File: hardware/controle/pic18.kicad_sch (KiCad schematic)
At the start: 10 parts, among them J10 Conn_01x05_Pin, J11 PWM, J12 ADC, U5 PIC18F05Q40

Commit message: controle: - pass ERC - adjust some components and connections - place components on board
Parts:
- J10: footprint conn-local:Molex_Pico-SPOX-5-Vertical -> Connector_PinHeader_2.54mm:PinHeader_1x05_P2.54mm_Horizontal
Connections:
- net +3.3V: now also J10.2 (Pin_2); no longer J10.5 (Pin_5)
- net GND: now also J10.3 (Pin_3); no longer J10.2 (Pin_2)
- net PGC: now also J10.5 (Pin_5); no longer J10.3 (Pin_3)
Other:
- moved on the sheet: J10, R20
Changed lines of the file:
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@@
 	)
 	(junction
-		(at 116.84 83.82)
+		(at 106.68 83.82)
 		(diameter 0)
 		(color 0 0 0 0)
 	)
 	(junction
-		(at 114.3 92.71)
+		(at 106.68 95.25)
+		(diameter 0)
+		(color 0 0 0 0)
+	)
+	(junction
+		(at 111.76 95.25)
 		(diameter 0)
 		(color 0 0 0 0)
@@
 	)
 	(junction
-		(at 109.22 88.9)
-		(diameter 0)
-		(color 0 0 0 0)
-	)
-	(junction
 		(at 157.48 88.9)
 		(diameter 0)
@@
 	(wire
 		(pts
-			(xy 116.84 83.82) (xy 157.48 83.82)
-		)
-		(stroke
-			(width 0)
-			(type default)
-		)
-	)
-	(wire
-		(pts
 			(xy 118.11 137.16) (xy 110.49 137.16)
 		)
@@
 	(wire
 		(pts
-			(xy 114.3 104.14) (xy 114.3 92.71)
-		)
-		(stroke
-			(width 0)
-			(type default)
-		)
-	)
-	(wire
-		(pts
 			(xy 93.98 111.76) (xy 140.97 111.76)
 		)
@@
 	(wire
 		(pts
-			(xy 140.97 106.68) (xy 111.76 106.68)
+			(xy 140.97 106.68) (xy 114.3 106.68)
 		)
 		(stroke
@@
 	(wire
 		(pts
-			(xy 109.22 92.71) (xy 109.22 88.9)
-		)
-		(stroke
-			(width 0)
-			(type default)
-		)
-	)
-	(wire
-		(pts
 			(xy 93.98 88.9) (xy 99.06 88.9)
 		)
@@
 	(wire
 		(pts
+			(xy 104.14 80.01) (xy 93.98 80.01)
+		)
+		(stroke
+			(width 0)
+			(type default)
+		)
+	)
+	(wire
+		(pts
 			(xy 104.14 88.9) (xy 106.68 88.9)
 		)
@@
 	(wire
 		(pts
-			(xy 106.68 80.01) (xy 93.98 80.01)
-		)
-		(stroke
-			(width 0)
-			(type default)
-		)
-	)
-	(wire
-		(pts
 			(xy 118.11 132.08) (xy 118.11 137.16)
 		)
@@
 	(wire
 		(pts
-			(xy 106.68 88.9) (xy 106.68 92.71)
-		)
-		(stroke
-			(width 0)
-			(type default)
-		)
-	)
-	(wire
-		(pts
-			(xy 116.84 80.01) (xy 116.84 83.82)
+			(xy 106.68 83.82) (xy 157.48 83.82)
+		)
+		(stroke
+			(width 0)
+			(type default)
+		)
+	)
+	(wire
+		(pts
+			(xy 106.68 88.9) (xy 106.68 95.25)
+		)
+		(stroke
+			(width 0)
+			(type default)
+		)
+	)
+	(wire
+		(pts
+			(xy 114.3 80.01) (xy 114.3 106.68)
+		)
+		(stroke
+			(width 0)
+			(type default)
+		)
+	)
+	(wire
+		(pts
+			(xy 111.76 104.14) (xy 140.97 104.14)
+		)
+		(stroke
+			(width 0)
+			(type default)
+		)
+	)
+	(wire
+		(pts
+			(xy 106.68 80.01) (xy 106.68 83.82)
+		)
+		(stroke
+			(width 0)
+			(type default)
+		)
+	)
+	(wire
+		(pts
+			(xy 109.22 80.01) (xy 109.22 88.9)
 		)
 		(stroke
@@
 	(wire
 		(pts
-			(xy 140.97 104.14) (xy 114.3 104.14)
+			(xy 106.68 95.25) (xy 106.68 99.06)
 		)
 		(stroke
@@
 	(wire
 		(pts
-			(xy 111.76 80.01) (xy 111.76 106.68)
-		)
-		(stroke
-			(width 0)
-			(type default)
-		)
-	)
-	(wire
-		(pts
-			(xy 114.3 92.71) (xy 114.3 80.01)
+			(xy 111.76 104.14) (xy 111.76 95.25)
 		)
 		(stroke
@@
 	(wire
 		(pts
-			(xy 104.14 83.82) (xy 116.84 83.82)
+			(xy 111.76 80.01) (xy 111.76 95.25)
+		)
+		(stroke
+			(width 0)
+			(type default)
+		)
+	)
+	(wire
+		(pts
+			(xy 104.14 83.82) (xy 106.68 83.82)
 		)
 		(stroke
@@
 		(pts
 			(xy 93.98 83.82) (xy 99.06 83.82)
-		)
-		(stroke
-			(width 0)
-			(type default)
-		)
-	)
-	(wire
-		(pts
-			(xy 109.22 88.9) (xy 109.22 80.01)
 		)
 		(stroke
@@
 	)
 	(symbol
-		(lib_id "centrale-rescue:GND-power")
+		(lib_id "power:GND")
 		(at 116.84 139.7 90)
 		(unit 1)
@@
 					(size 1.27 1.27)
 				)
+				(hide yes)
 			)
 		)
@@
 					(size 1.27 1.27)
 				)
-			)
-		)
-		(property "Description" ""
+				(hide yes)
+			)
+		)
+		(property "Description" "Power symbol creates a global label with name \"GND\" , ground"
 			(at 116.84 139.7 0)
 			(effects
@@
 	(symbol
 		(lib_id "power:GND")
-		(at 106.68 92.71 0)
+		(at 106.68 99.06 0)
 		(unit 1)
 		(exclude_from_sim no)
@@
 		(fields_autoplaced yes)
 		(property "Reference" "#PWR023"
+			(at 106.68 105.41 0)
+			(effects
+				(font
+					(size 1.27 1.27)
+				)
+				(hide yes)
+			)
+		)
+		(property "Value" "GND"
+			(at 106.68 102.2349 90)
+			(effects
+				(font
+					(size 1.27 1.27)
+				)
+				(justify right)
+			)
+		)
+		(property "Footprint" ""
 			(at 106.68 99.06 0)
 			(effects
@@
 			)
 		)
-		(property "Value" "GND"
-			(at 106.68 95.8849 90)
-			(effects
-				(font
-					(size 1.27 1.27)
-				)
-				(justify right)
-			)
-		)
-		(property "Footprint" ""
-			(at 106.68 92.71 0)
-			(effects
-				(font
-					(size 1.27 1.27)
-				)
-				(hide yes)
-			)
-		)
 		(property "Datasheet" ""
-			(at 106.68 92.71 0)
+			(at 106.68 99.06 0)
 			(effects
 				(font
@@
 		)
 		(property "Description" "Power symbol creates a global label with name \"GND\" , ground"
-			(at 106.68 92.71 0)
+			(at 106.68 99.06 0)
 			(effects
 				(font
@@
 		)
 		(property "P/N" ""
-			(at 106.68 92.71 0)
+			(at 106.68 99.06 0)
 			(effects
 				(font
@@
 	(symbol
 		(lib_id "Connector:Conn_01x05_Pin")
-		(at 111.76 74.93 90)
+		(at 109.22 74.93 90)
 		(mirror x)
 		(unit 1)
@@
 		(dnp no)
 		(property "Reference" "J10"
-			(at 112.9722 74.2188 0)
+			(at 110.4322 74.2188 0)
 			(effects
 				(font
@@
 		)
 		(property "Value" "Conn_01x05_Pin"
-			(at 110.5479 74.2188 0)
+			(at 108.0079 74.2188 0)
 			(effects
 				(font
@@
 			)
 		)
-		(property "Footprint" "conn-local:Molex_Pico-SPOX-5-Vertical"
-			(at 111.76 74.93 0)
+		(property "Footprint" "Connector_PinHeader_2.54mm:PinHeader_1x05_P2.54mm_Horizontal"
+			(at 109.22 74.93 0)
 			(effects
 				(font
@@
 		)
 		(property "Datasheet" "~"
-			(at 111.76 74.93 0)
+			(at 109.22 74.93 0)
 			(effects
 				(font
@@
 		)
 		(property "Description" "Generic connector, single row, 01x05, script generated"
-			(at 111.76 74.93 0)
+			(at 109.22 74.93 0)
 			(effects
 				(font
@@
 		)
 		(property "P/N" "87437-0543"
-			(at 111.76 74.93 0)
+			(at 109.22 74.93 0)
 			(effects
 				(font
@@
 	)
 	(symbol
-		(lib_id "centrale-rescue:+3.3V-power")
+		(lib_id "power:+3.3V")
 		(at 130.81 142.24 270)
 		(unit 1)
@@
 			)
 		)
-		(property "Description" ""
+		(property "Description" "Power symbol creates a global label with name \"+3.3V\""
 			(at 130.81 142.24 0)
 			(effects
@@
 	(symbol
 		(lib_id "Device:R_Small")
-		(at 111.76 92.71 270)
+		(at 109.22 95.25 270)
 		(unit 1)
 		(exclude_from_sim no)
@@
 		(dnp no)
 		(property "Reference" "R20"
-			(at 111.76 94.742 90)
+			(at 109.22 97.282 90)
 			(effects
 				(font
@@
 		)
 		(property "Value" "10K"
-			(at 111.7854 92.8878 90)
+			(at 109.2454 95.4278 90)
 			(effects
 				(font
@@
 		)
 		(property "Footprint" "Resistor_SMD:R_0805_2012Metric_Pad1.20x1.40mm_HandSolder"
-			(at 111.76 90.932 90)
+			(at 109.22 93.472 90)
 			(effects
 				(font
@@
 		)
 		(property "Datasheet" "~"
-			(at 111.76 92.71 0)
+			(at 109.22 95.25 0)
 			(effects
 				(font
@@
 		)
 		(property "Description" "Resistor, small symbol"
-			(at 111.76 92.71 0)
+			(at 109.22 95.25 0)
 			(effects
 				(font
@@
 		)
 		(property "P/N" "stock"
-			(at 111.76 92.71 0)
+			(at 109.22 95.25 0)
 			(effects
 				(font
@@
 	)
 	(symbol
-		(lib_id "centrale-rescue:+3.3V-power")
+		(lib_id "power:+3.3V")
 		(at 113.03 142.24 270)
 		(unit 1)
@@
 			)
 		)
-		(property "Description" ""
+		(property "Description" "Power symbol creates a global label with name \"+3.3V\""
 			(at 113.03 142.24 0)
 			(effects
@@
 	)
 	(symbol
-		(lib_id "centrale-rescue:GND-power")
+		(lib_id "power:GND")
 		(at 134.62 139.7 90)
 		(unit 1)
@@
 					(size 1.27 1.27)
 				)
+				(hide yes)
 			)
 		)
@@
 					(size 1.27 1.27)
 				)
-			)
-		)
-		(property "Description" ""
+				(hide yes)
+			)
+		)
+		(property "Description" "Power symbol creates a global label with name \"GND\" , ground"
 			(at 134.62 139.7 0)
 			(effects

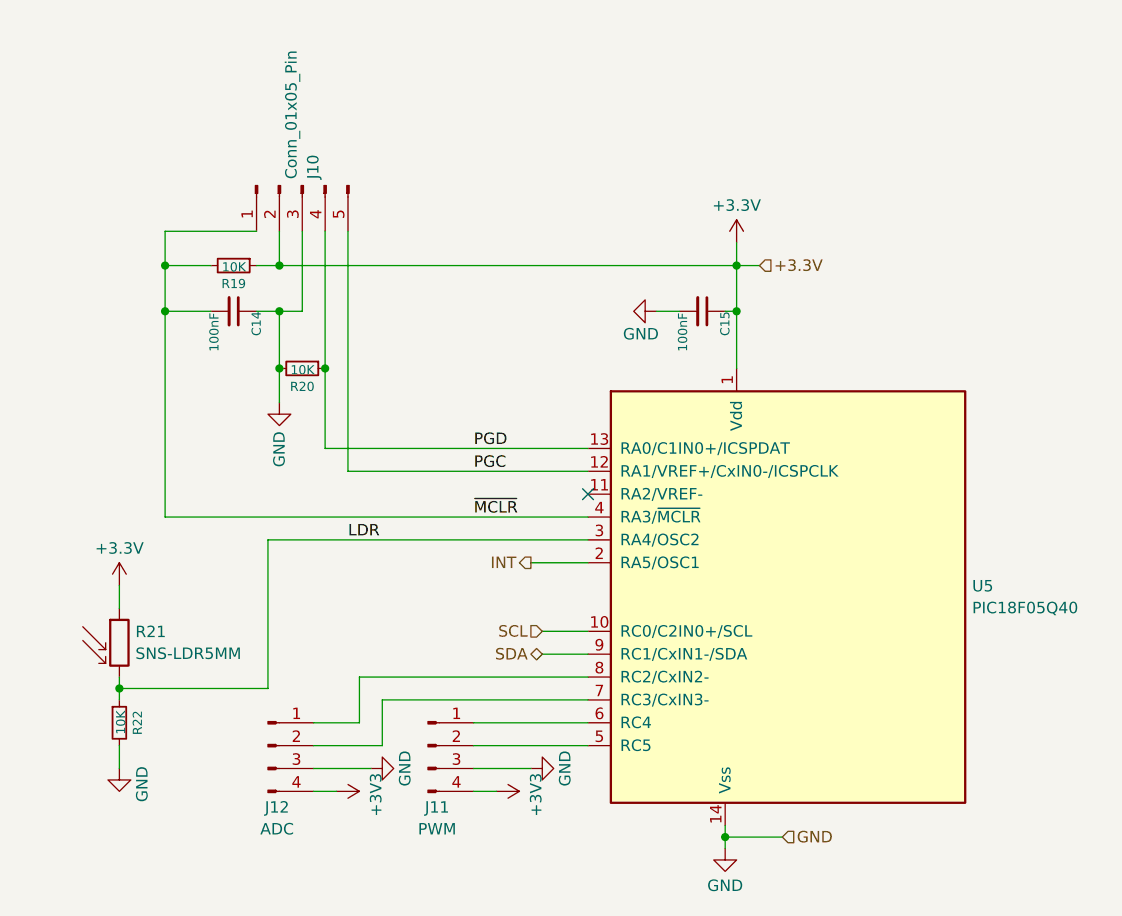
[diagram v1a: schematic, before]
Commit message: hardware/controle: control CPU power from pic18: - add a separate 3.3V power for pic18 - use the pic18 to start the tps54228
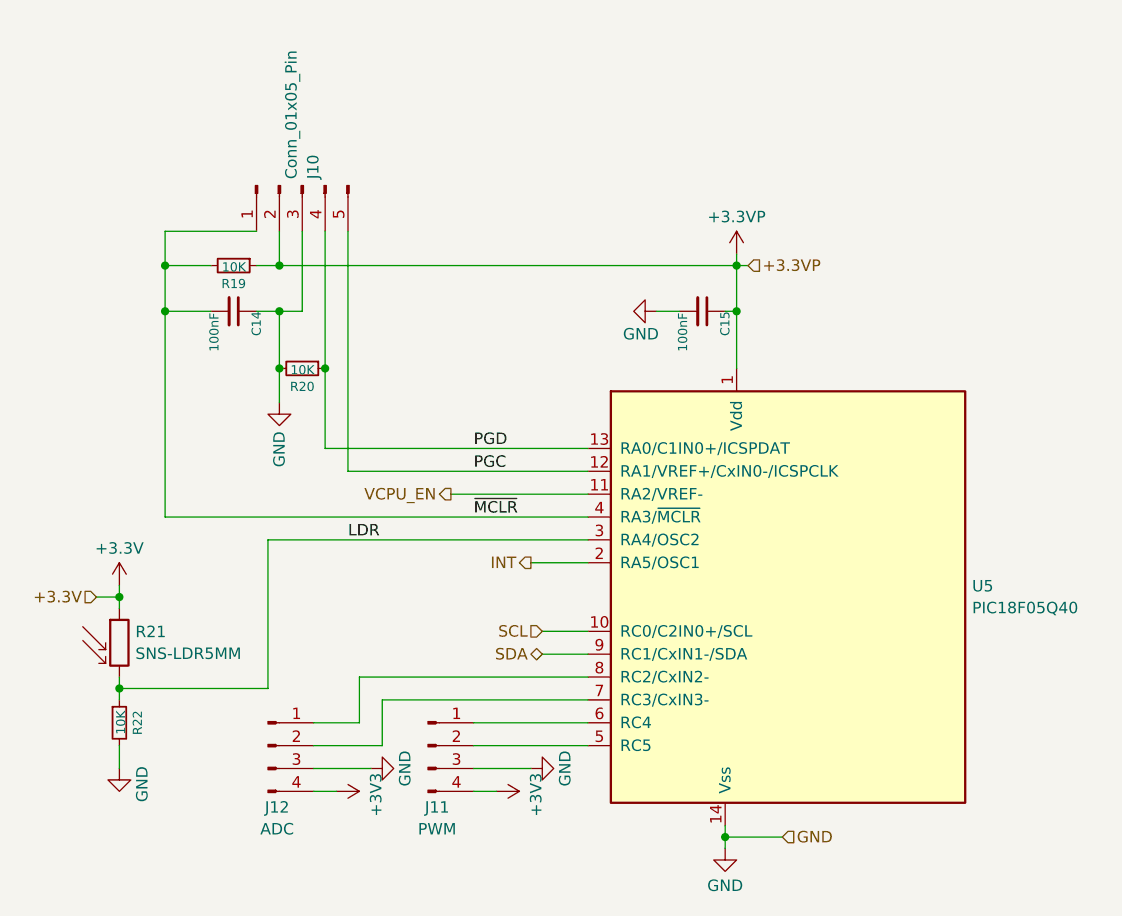
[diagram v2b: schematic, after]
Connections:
- net +3.3V: no longer C15.1, J10.2 (Pin_2), R19.1, U5.1 (Vdd)
- net VCPU_EN: now reaches U5.11 (RA2/VREF-)
- new net +3.3VP: C15.1, J10.2 (Pin_2), R19.1, U5.1 (Vdd)
- no-connect marks 1 -> 0
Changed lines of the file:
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@@
 	(paper "A4")
+	(junction
+		(at 157.48 83.82)
+		(diameter 0)
+		(color 0 0 0 0)
+	)
 	(junction
 		(at 93.98 83.82)
@@
 	)
 	(junction
-		(at 157.48 88.9)
+		(at 88.9 120.65)
 		(diameter 0)
 		(color 0 0 0 0)
 	)
 	(junction
-		(at 157.48 83.82)
+		(at 157.48 88.9)
 		(diameter 0)
 		(color 0 0 0 0)
@@
 		(color 0 0 0 0)
 	)
-	(no_connect
-		(at 140.97 109.22)
-	)
 	(wire
 		(pts
@@
 	(wire
 		(pts
-			(xy 157.48 83.82) (xy 160.02 83.82)
+			(xy 88.9 120.65) (xy 86.36 120.65)
 		)
 		(stroke
@@
 	(wire
 		(pts
+			(xy 88.9 120.65) (xy 88.9 121.92)
+		)
+		(stroke
+			(width 0)
+			(type default)
+		)
+	)
+	(wire
+		(pts
 			(xy 105.41 130.81) (xy 88.9 130.81)
 		)
@@
 	(wire
 		(pts
+			(xy 157.48 82.55) (xy 157.48 83.82)
+		)
+		(stroke
+			(width 0)
+			(type default)
+		)
+	)
+	(wire
+		(pts
 			(xy 134.62 116.84) (xy 140.97 116.84)
 		)
@@
 	(wire
 		(pts
+			(xy 125.73 109.22) (xy 140.97 109.22)
+		)
+		(stroke
+			(width 0)
+			(type default)
+		)
+	)
+	(wire
+		(pts
 			(xy 106.68 88.9) (xy 106.68 95.25)
 		)
@@
 	(wire
 		(pts
-			(xy 157.48 81.28) (xy 157.48 83.82)
-		)
-		(stroke
-			(width 0)
-			(type default)
-		)
-	)
-	(wire
-		(pts
 			(xy 88.9 137.16) (xy 88.9 139.7)
 		)
@@
 	(wire
 		(pts
-			(xy 88.9 119.38) (xy 88.9 121.92)
+			(xy 88.9 119.38) (xy 88.9 120.65)
 		)
 		(stroke
@@
 		(pts
 			(xy 93.98 88.9) (xy 93.98 111.76)
+		)
+		(stroke
+			(width 0)
+			(type default)
+		)
+	)
+	(wire
+		(pts
+			(xy 157.48 83.82) (xy 158.75 83.82)
 		)
 		(stroke
@@
 	(hierarchical_label "+3.3V"
 		(shape input)
-		(at 160.02 83.82 0)
+		(at 86.36 120.65 180)
 		(fields_autoplaced yes)
 		(effects
@@
 				(size 1.27 1.27)
 			)
+			(justify right)
+		)
+	)
+	(hierarchical_label "+3.3VP"
+		(shape input)
+		(at 158.75 83.82 0)
+		(fields_autoplaced yes)
+		(effects
+			(font
+				(size 1.27 1.27)
+			)
 			(justify left)
+		)
+	)
+	(hierarchical_label "VCPU_EN"
+		(shape output)
+		(at 125.73 109.22 180)
+		(fields_autoplaced yes)
+		(effects
+			(font
+				(size 1.27 1.27)
+			)
+			(justify right)
 		)
 	)
@@
 	(symbol
 		(lib_id "power:+3.3V")
-		(at 157.48 81.28 0)
+		(at 157.48 82.55 0)
 		(unit 1)
 		(exclude_from_sim no)
@@
 		(fields_autoplaced yes)
 		(property "Reference" "#PWR024"
-			(at 157.48 85.09 0)
-			(effects
-				(font
-					(size 1.27 1.27)
-				)
-				(hide yes)
-			)
-		)
-		(property "Value" "+3.3V"
-			(at 157.48 77.1469 0)
+			(at 157.48 86.36 0)
+			(effects
+				(font
+					(size 1.27 1.27)
+				)
+				(hide yes)
+			)
+		)
+		(property "Value" "+3.3VP"
+			(at 157.48 78.4169 0)
 			(effects
 				(font
@@
 		)
 		(property "Footprint" ""
-			(at 157.48 81.28 0)
+			(at 157.48 82.55 0)
 			(effects
 				(font
@@
 		)
 		(property "Datasheet" ""
-			(at 157.48 81.28 0)
+			(at 157.48 82.55 0)
 			(effects
 				(font
@@
 		)
 		(property "Description" "Power symbol creates a global label with name \"+3.3V\""
-			(at 157.48 81.28 0)
+			(at 157.48 82.55 0)
 			(effects
 				(font
@@
 		)
 		(property "P/N" ""
-			(at 157.48 81.28 0)
-			(effects
-				(font
+			(at 157.48 82.55 0)
+			(effects
+				(font
